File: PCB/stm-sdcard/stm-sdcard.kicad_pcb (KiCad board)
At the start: 2 copper layers, 80.6 x 40 mm, 31 parts, among them J1 Conn_01x04_Pin, J2 Conn_01x03_Pin, SW1 SW_Push, SW2 SW_Push, U1 HX TF-CARD H1.8, U2 HX TF-CARD H1.8, U3 Conn_01x06_Pin, U4 TLV1117LV33DCYR

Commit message: routing started
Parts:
- added REF**: MountingHole_2.5mm_Pad_TopOnly, MountingHole:MountingHole_2.5mm_Pad_TopOnly, F.Cu at (103.0, 107.0)
- added REF**: MountingHole_2.5mm_Pad_TopOnly, MountingHole:MountingHole_2.5mm_Pad_TopOnly, F.Cu at (167.0, 107.0)
- added REF**: MountingHole_2.5mm_Pad_TopOnly, MountingHole:MountingHole_2.5mm_Pad_TopOnly, F.Cu at (167.0, 73.0)
- added REF**: MountingHole_2.5mm_Pad_TopOnly, MountingHole:MountingHole_2.5mm_Pad_TopOnly, F.Cu at (103.0, 73.0)
- moved UART_PRG1 14.2 mm to (162.5, 78.4)
- moved C2 13.3 mm to (106.0, 92.0), turned to 90 degrees
- moved U4 5.85 mm to (112.0, 92.0), turned to 180 degrees
- moved R1 5.59 mm to (109.0, 85.0), turned to -90 degrees
- moved USB1 5.51 mm to (103.6, 82.5)
- moved SWD_PRG1 5.19 mm to (168.0, 78.3)
- moved R2 4.61 mm to (109.0, 80.5), turned to 90 degrees
- moved JP1 4.42 mm to (102.0, 90.4)
- moved BAT1 4.22 mm to (102.0, 99.2)
- moved SPI2 3.05 mm to (151.9, 103.0)
- moved SPI3 2.63 mm to (108.3, 108.0)
- moved SPI1 2.55 mm to (133.4, 103.0)
- moved C1 1.00 mm to (115.5, 87.5), turned to 90 degrees
- moved C7 1.00 mm to (138.0, 90.5)
- moved C8 1.00 mm to (136.0, 90.5)
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- renumbered ADC1_CONN1 to ADC1, ADC2_CONN1 to ADC2, BAT_CONN1 to BAT1, DAC1_CONN1 to DAC1, OPAMP3_OUT_CONN1 to OPA3, U1 to SPI1, U2 to SPI2, U3 to SPI3, USART1_CONN1 to USART1
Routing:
- added copper zone on B.Cu, net GND
- added copper zone on F.Cu, net GND
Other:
- board size 80.6 x 40 mm -> 70 x 40 mm

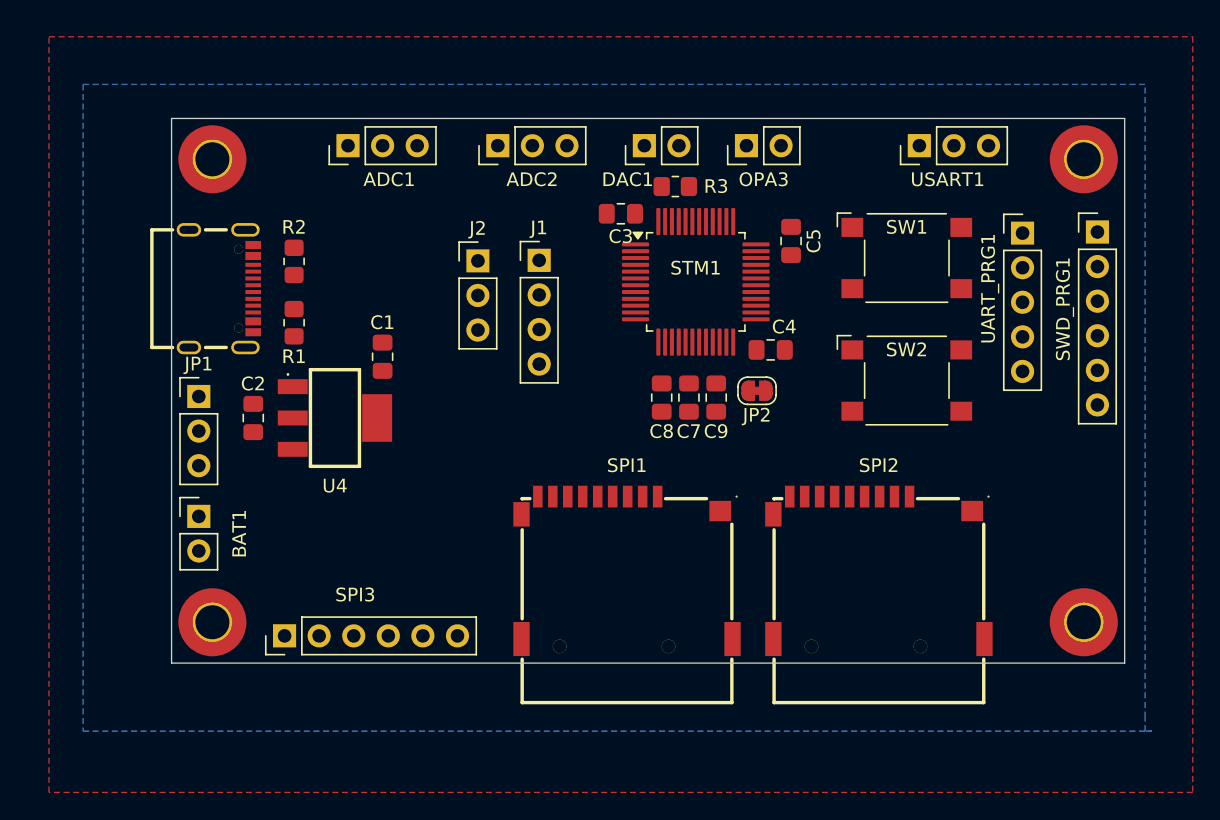
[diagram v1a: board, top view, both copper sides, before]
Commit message: Routing done, errors corrected
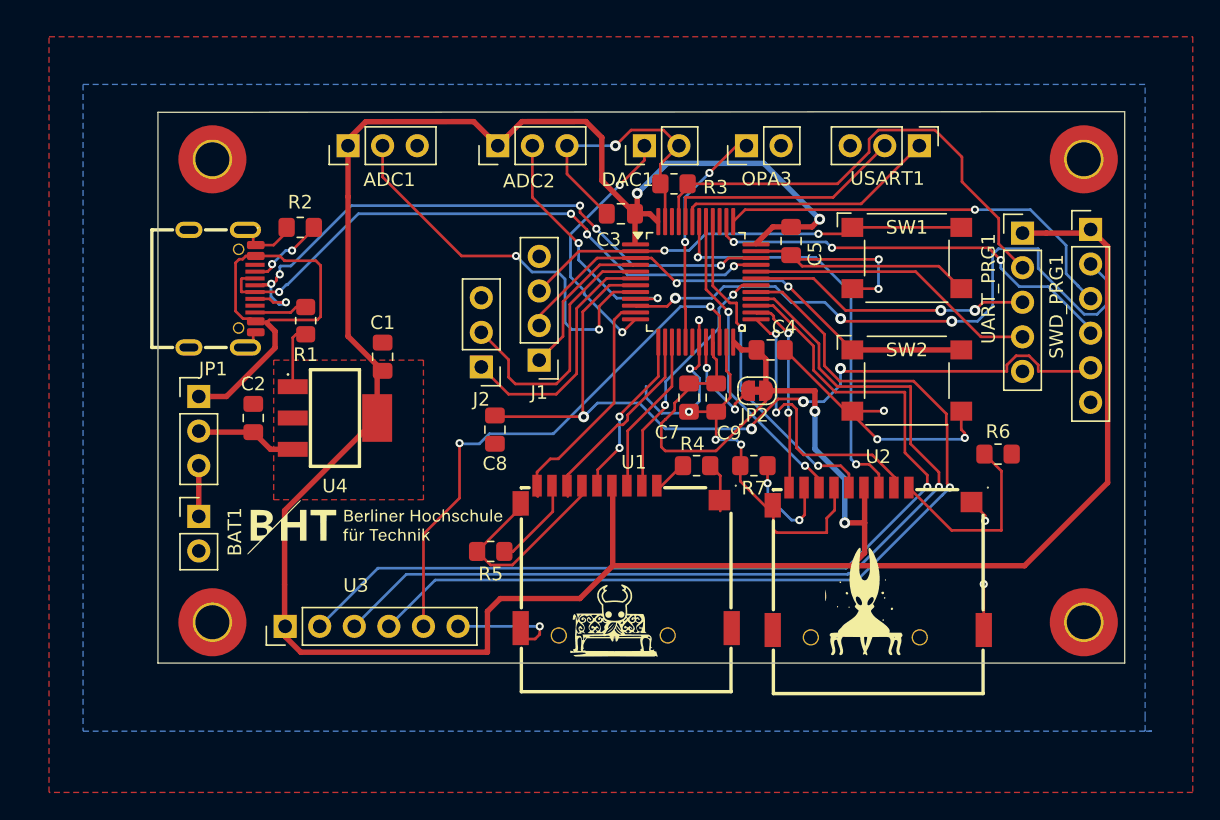
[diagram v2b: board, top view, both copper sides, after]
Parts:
- added G***: LOGO, LOGO, F.Cu at (151.0, 105.5)
- added G***: LOGO, LOGO, F.Cu at (132.8, 107.2)
- added G***: LOGO, LOGO, F.Cu at (115.0, 99.9)
- added R4: 50k, Resistor_SMD:R_0805_2012Metric_Pad1.20x1.40mm_HandSolder, F.Cu at (138.6, 95.5)
- added R5: 50k, Resistor_SMD:R_0805_2012Metric_Pad1.20x1.40mm_HandSolder, F.Cu at (123.4, 101.8)
- added R6: 50k, Resistor_SMD:R_0805_2012Metric_Pad1.20x1.40mm_HandSolder, F.Cu at (160.7, 94.7)
- added R7: 50k, Resistor_SMD:R_0805_2012Metric_Pad1.20x1.40mm_HandSolder, F.Cu at (142.8, 95.5)
- moved C8 12.5 mm to (123.8, 92.8)
- moved J2 7.79 mm to (122.8, 88.2), turned to 180 degrees
- moved J1 7.33 mm to (127.0, 87.8), turned to 180 degrees
- moved R2 2.54 mm to (109.5, 78.0), turned to 180 degrees
- moved R1 0.86 mm to (109.8, 84.8)
- moved U1 0.80 mm to (133.4, 102.2)
- moved U3 0.70 mm to (108.3, 107.3)
- moved U2 0.66 mm to (151.9, 102.3)
- moved SWD_PRG1 0.53 mm to (167.5, 78.2)
- moved R3 0.22 mm to (136.9, 74.8)
- turned USART1 to -90 degrees
- renumbered SPI1 to U1, SPI2 to U2, SPI3 to U3
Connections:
- U1 pad 1: /PA15_PU1 -> /SPI-SDcard/PULLUP1
- U1 pad 8: /PB0_PU2 -> /SPI-SDcard/PULLUP2
- U2 pad 1: /PB2_PU3 -> /SPI-SDcard/PULLUP3
- U2 pad 8: /PB9_PU4 -> /SPI-SDcard/PULLUP4
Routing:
- net +3.3V: track 0.00 -> 241.0 mm, vias 0 -> 4
- net GND: track 0.00 -> 154.7 mm, vias 0 -> 14
- net /PB13: track 0.00 -> 71.1 mm, vias 0 -> 1
- net /PB14: track 0.00 -> 70.5 mm, vias 0 -> 1
- net /PB15: track 0.00 -> 70.0 mm, vias 0 -> 1
- net /PG10_nRST: track 0.00 -> 61.9 mm, vias 0 -> 4
- net /PA2_VCP_Tx: track 0.00 -> 47.6 mm, vias 0 -> 3
- net /USB_D+: track 0.00 -> 47.0 mm, vias 0 -> 6
- net /USB_D-: track 0.00 -> 44.4 mm, vias 0 -> 4
- net /PB10: track 0.00 -> 40.1 mm, vias 0 -> 2
- net /PC14: track 0.00 -> 36.4 mm, vias 0 -> 2
- net /PB8_BOOT0: track 0.00 -> 36.0 mm
- net /PC13: track 0.00 -> 32.9 mm, vias 0 -> 2
- net /PB5: track 0.00 -> 31.7 mm, vias 0 -> 2
- net /PA14_SWDCLK: track 0.00 -> 31.7 mm, vias 0 -> 3
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- added copper zone on F.Cu, net +3.3V
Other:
- board size 70 x 40 mm -> 71 x 40.5 mm

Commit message: gerber files exported, ordering now
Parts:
- added GND: TestPoint_Bridge_Pitch2.0mm_Drill0.7mm, TestPoint:TestPoint_Bridge_Pitch2.0mm_Drill0.7mm, F.Cu at (109.5, 71.8)
- added GND: TestPoint_Bridge_Pitch2.0mm_Drill0.7mm, TestPoint:TestPoint_Bridge_Pitch2.0mm_Drill0.7mm, F.Cu at (168.2, 102.7)
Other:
- board text added: "CS"
- board text added: "MISO"
- board text added: "MOSI"
- board text added: "SCK"
